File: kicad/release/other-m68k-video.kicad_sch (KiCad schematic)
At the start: 27 parts, among them J5 RCA composite, U11 AD724JR, Y2 3.579545MHz

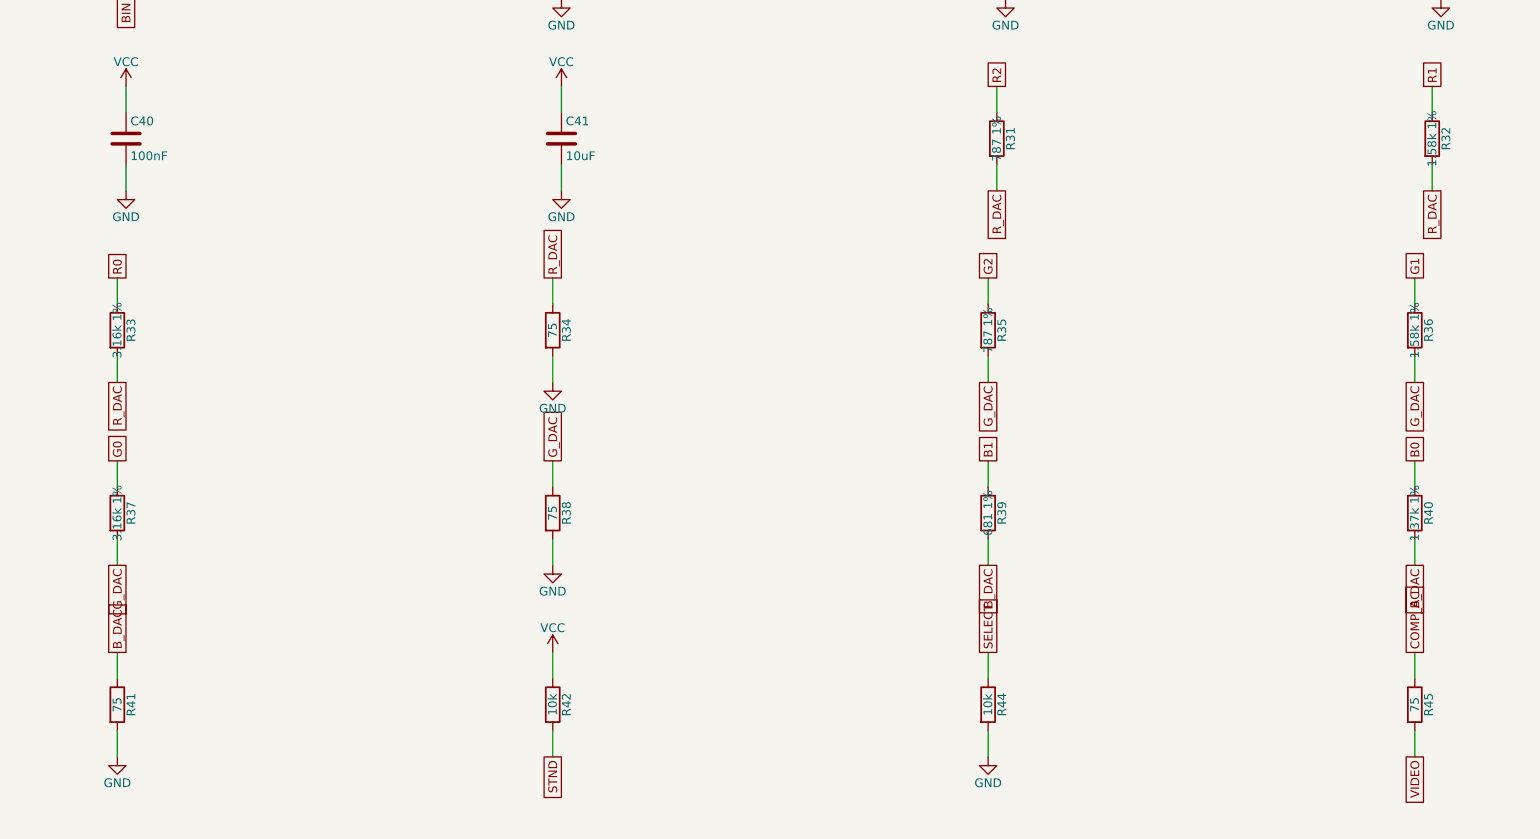
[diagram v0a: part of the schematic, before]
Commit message: KiCad rev C1: native 4-bit SD bus (CLK, CMD, DAT0..3 straight from CPLD2 with 10 k pull-ups to 3.3 V, the three 1.8k/3.3k dividers removed, DAT1/DAT2 on CPLD2 pins 16/58), UIO0..3 removed from J8 (pins 5/7/9/11 n/c); ERC 0, DRC 0, rerouted (22 passes, 0 unrouted, 5146 segments, 530 vias); fab package and release snapshot regenerated; ORDER.md notes rev C1 vs the ordered B4
Co-Authored-By: Claude Fable 5.1 <noreply@anthropic.com>
Claude-Session: https://claude.ai/code/session_019bbFLKMxhKXGW6aABP44Z1
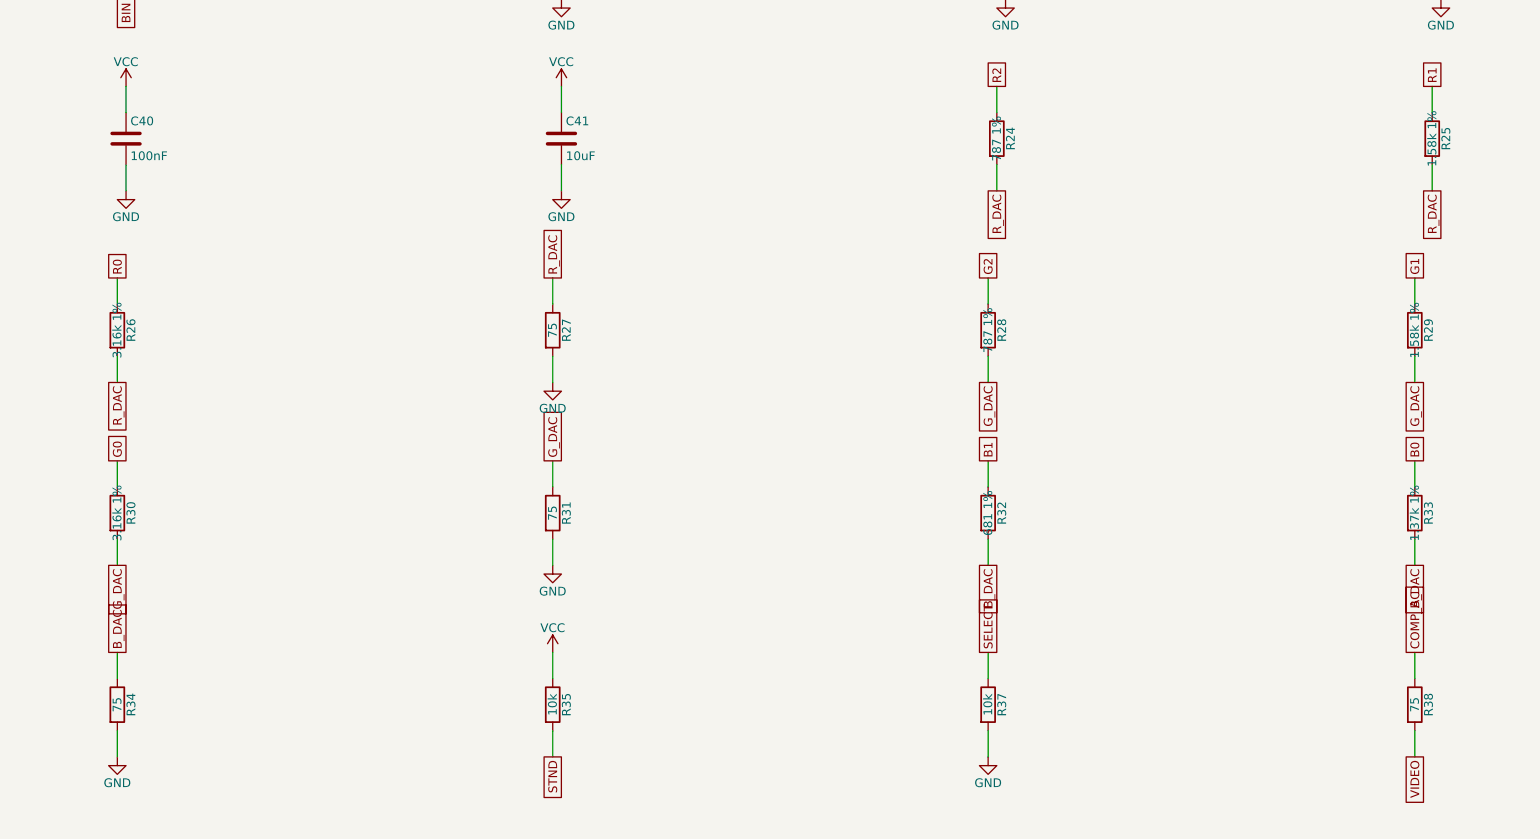
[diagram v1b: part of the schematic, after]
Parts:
- removed R36: 1.58k 1%, Resistor_SMD:R_0603_1608Metric, symbol Device:R
- removed R39: 681 1%, Resistor_SMD:R_0603_1608Metric, symbol Device:R
- removed R40: 1.37k 1%, Resistor_SMD:R_0603_1608Metric, symbol Device:R
- removed R41, R45: 75, Resistor_SMD:R_0603_1608Metric, symbol Device:R
- removed R42, R44: 10k, Resistor_SMD:R_0603_1608Metric, symbol Device:R
- added R24, R28: 787 1%, Resistor_SMD:R_0603_1608Metric, symbol Device:R
- added R25, R29: 1.58k 1%, Resistor_SMD:R_0603_1608Metric, symbol Device:R
- added R26, R30: 3.16k 1%, Resistor_SMD:R_0603_1608Metric, symbol Device:R
- added R27: 75, Resistor_SMD:R_0603_1608Metric, symbol Device:R
- R31: value 787 1% -> 75; Desc 787 ohm 1% 0603 (DAC) -> 75 ohm 1% 0603; MPN RC0603FR-07787RL -> RC0603FR-0775RL
- R32: value 1.58k 1% -> 681 1%; Desc 1.58 k 1% 0603 (DAC) -> 681 ohm 1% 0603 (DAC); MPN RC0603FR-071K58L -> RC0603FR-07681RL
- R33: value 3.16k 1% -> 1.37k 1%; Desc 3.16 k 1% 0603 (DAC) -> 1.37 k 1% 0603 (DAC); MPN RC0603FR-073K16L -> RC0603FR-071K37L
- R35: value 787 1% -> 10k; Desc 787 ohm 1% 0603 (DAC) -> 10 k 1% 0603; LCSC (none) -> C25804; MPN RC0603FR-07787RL -> RC0603FR-0710KL
- R37: value 3.16k 1% -> 10k; Desc 3.16 k 1% 0603 (DAC) -> 10 k 1% 0603; LCSC (none) -> C25804; MPN RC0603FR-073K16L -> RC0603FR-0710KL
- R38: PcbNear U11 -> J5
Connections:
- net B0: now also R33.1
- net B1: now also R32.1
- net B_DAC: now also R32.2, R33.2, R34.1
- net COMP_AC: now also R38.1
- net G0: now also R30.1; no longer R37.1
- net G1: now also R29.1
- net G2: now also R28.1; no longer R35.1
- net GND: now also R31.2, R37.2, R27.2; no longer R38.2
- net G_DAC: now also R31.1, R28.2, R29.2, R30.2; no longer R35.2, R37.2, R38.1
- net R0: now also R26.1; no longer R33.1
- net R1: now also R25.1; no longer R32.1
- net R2: now also R24.1; no longer R31.1
- net R_DAC: now also R24.2, R25.2, R26.2, R27.1; no longer R31.2, R32.2, R33.2, R34.1
- net SELECT: now also R37.1
- net STND: now also R35.2
- net VCC: now also R35.1
- net VIDEO: now also R38.2
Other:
- moved on the sheet: R31, R32, R33, R34, R35, R37, R38
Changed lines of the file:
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@@
 	(title_block
 		(title "video")
-		(rev "A")
+		(rev "C1")
 		(comment 1 "generated by kicad/gen_sch.py - do not edit")
 	)
@@
 		(on_board yes)
 		(dnp no)
-		(property "Reference" "R45"
+		(property "Reference" "R38"
 			(at 236.982 220.98 90)
 			(effects
@@
 			(project "other-m68k"
 				(path "/0bd472a6-02e9-5c95-a886-c7baf9734bb2/8a9b6c11-c190-5532-a52c-e2ee2f3a56d6"
-					(reference "R45")
+					(reference "R38")
 					(unit 1)
 				)
@@
 		(on_board yes)
 		(dnp no)
-		(property "Reference" "R44"
+		(property "Reference" "R37"
 			(at 174.752 220.98 90)
 			(effects
@@
 			(project "other-m68k"
 				(path "/0bd472a6-02e9-5c95-a886-c7baf9734bb2/8a9b6c11-c190-5532-a52c-e2ee2f3a56d6"
-					(reference "R44")
+					(reference "R37")
 					(unit 1)
 				)
@@
 		(on_board yes)
 		(dnp no)
-		(property "Reference" "R42"
+		(property "Reference" "R35"
 			(at 111.252 220.98 90)
 			(effects
@@
 			(project "other-m68k"
 				(path "/0bd472a6-02e9-5c95-a886-c7baf9734bb2/8a9b6c11-c190-5532-a52c-e2ee2f3a56d6"
-					(reference "R42")
+					(reference "R35")
 					(unit 1)
 				)
@@
 		(on_board yes)
 		(dnp no)
-		(property "Reference" "R41"
+		(property "Reference" "R34"
 			(at 47.752 220.98 90)
 			(effects
@@
 			(project "other-m68k"
 				(path "/0bd472a6-02e9-5c95-a886-c7baf9734bb2/8a9b6c11-c190-5532-a52c-e2ee2f3a56d6"
-					(reference "R41")
+					(reference "R34")
 					(unit 1)
 				)
@@
 		(on_board yes)
 		(dnp no)
-		(property "Reference" "R40"
+		(property "Reference" "R33"
 			(at 236.982 193.04 90)
 			(effects
@@
 			(project "other-m68k"
 				(path "/0bd472a6-02e9-5c95-a886-c7baf9734bb2/8a9b6c11-c190-5532-a52c-e2ee2f3a56d6"
-					(reference "R40")
+					(reference "R33")
 					(unit 1)
 				)
@@
 		(on_board yes)
 		(dnp no)
-		(property "Reference" "R39"
+		(property "Reference" "R32"
 			(at 174.752 193.04 90)
 			(effects
@@
 			(project "other-m68k"
 				(path "/0bd472a6-02e9-5c95-a886-c7baf9734bb2/8a9b6c11-c190-5532-a52c-e2ee2f3a56d6"
-					(reference "R39")
+					(reference "R32")
 					(unit 1)
 				)
@@
 		(on_board yes)
 		(dnp no)
-		(property "Reference" "R38"
+		(property "Reference" "R31"
 			(at 111.252 193.04 90)
 			(effects
@@
 			(project "other-m68k"
 				(path "/0bd472a6-02e9-5c95-a886-c7baf9734bb2/8a9b6c11-c190-5532-a52c-e2ee2f3a56d6"
-					(reference "R38")
+					(reference "R31")
 					(unit 1)
 				)
@@
 		(on_board yes)
 		(dnp no)
-		(property "Reference" "R37"
+		(property "Reference" "R30"
 			(at 47.752 193.04 90)
 			(effects
@@
 			(project "other-m68k"
 				(path "/0bd472a6-02e9-5c95-a886-c7baf9734bb2/8a9b6c11-c190-5532-a52c-e2ee2f3a56d6"
-					(reference "R37")
+					(reference "R30")
 					(unit 1)
 				)
@@
 		(on_board yes)
 		(dnp no)
-		(property "Reference" "R36"
+		(property "Reference" "R29"
 			(at 236.982 166.37 90)
 			(effects
@@
 			(project "other-m68k"
 				(path "/0bd472a6-02e9-5c95-a886-c7baf9734bb2/8a9b6c11-c190-5532-a52c-e2ee2f3a56d6"
-					(reference "R36")
+					(reference "R29")
 					(unit 1)
 				)
@@
 		(on_board yes)
 		(dnp no)
-		(property "Reference" "R35"
+		(property "Reference" "R28"
 			(at 174.752 166.37 90)
 			(effects
@@
 			(project "other-m68k"
 				(path "/0bd472a6-02e9-5c95-a886-c7baf9734bb2/8a9b6c11-c190-5532-a52c-e2ee2f3a56d6"
-					(reference "R35")
+					(reference "R28")
 					(unit 1)
 				)
@@
 		(on_board yes)
 		(dnp no)
-		(property "Reference" "R34"
+		(property "Reference" "R27"
 			(at 111.252 166.37 90)
 			(effects
@@
 			(project "other-m68k"
 				(path "/0bd472a6-02e9-5c95-a886-c7baf9734bb2/8a9b6c11-c190-5532-a52c-e2ee2f3a56d6"
-					(reference "R34")
+					(reference "R27")
 					(unit 1)
 				)
@@
 		(on_board yes)
 		(dnp no)
-		(property "Reference" "R33"
+		(property "Reference" "R26"
 			(at 47.752 166.37 90)
 			(effects
@@
 			(project "other-m68k"
 				(path "/0bd472a6-02e9-5c95-a886-c7baf9734bb2/8a9b6c11-c190-5532-a52c-e2ee2f3a56d6"
-					(reference "R33")
+					(reference "R26")
 					(unit 1)
 				)
@@
 		(on_board yes)
 		(dnp no)
-		(property "Reference" "R32"
+		(property "Reference" "R25"
 			(at 239.522 138.43 90)
 			(effects
@@
 			(project "other-m68k"
 				(path "/0bd472a6-02e9-5c95-a886-c7baf9734bb2/8a9b6c11-c190-5532-a52c-e2ee2f3a56d6"
-					(reference "R32")
+					(reference "R25")
 					(unit 1)
 				)
@@
 		(on_board yes)
 		(dnp no)
-		(property "Reference" "R31"
+		(property "Reference" "R24"
 			(at 176.022 138.43 90)
 			(effects
@@
 			(project "other-m68k"
 				(path "/0bd472a6-02e9-5c95-a886-c7baf9734bb2/8a9b6c11-c190-5532-a52c-e2ee2f3a56d6"
-					(reference "R31")
+					(reference "R24")
 					(unit 1)
 				)
